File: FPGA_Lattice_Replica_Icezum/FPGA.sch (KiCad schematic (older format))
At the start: 33 parts, among them U1 iCE40HX1K-TQ144, U2 N25Q032A

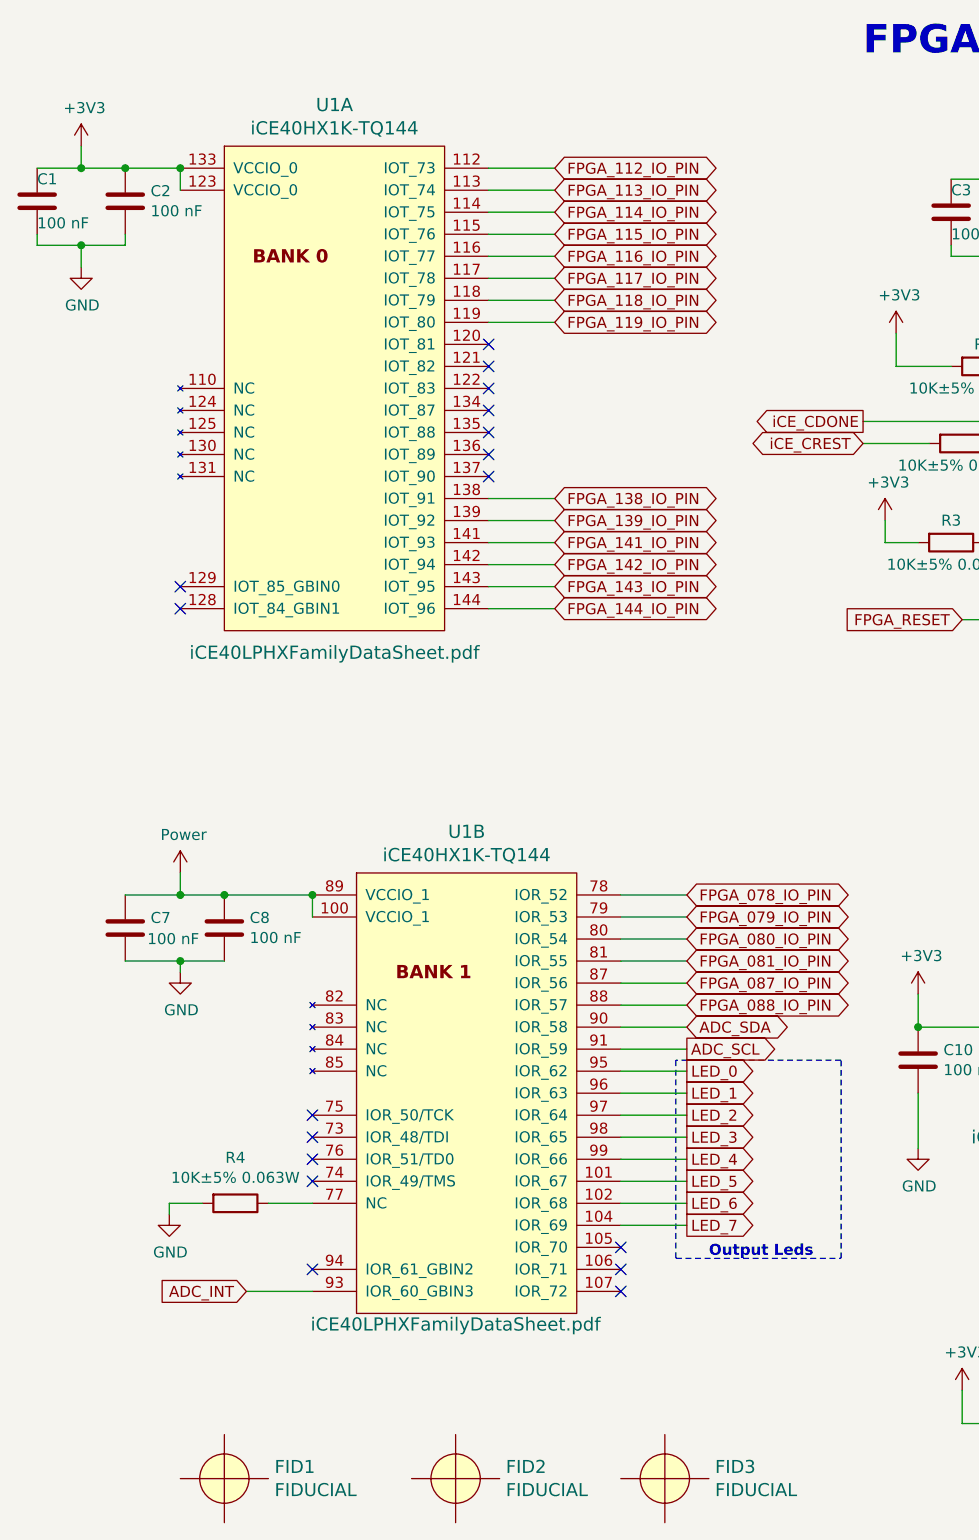
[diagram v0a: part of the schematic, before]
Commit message: se mejoro esquematico de acuerdo a la revisión del docente. Se mejoro rotulo (se coloco link del repo, autor y autor de la versión original y la licencia) se mejoro el flujo izquiera derecha de los botones, se desplazo fiduciales a la página principal, se achico el esquematico en la parte de headers
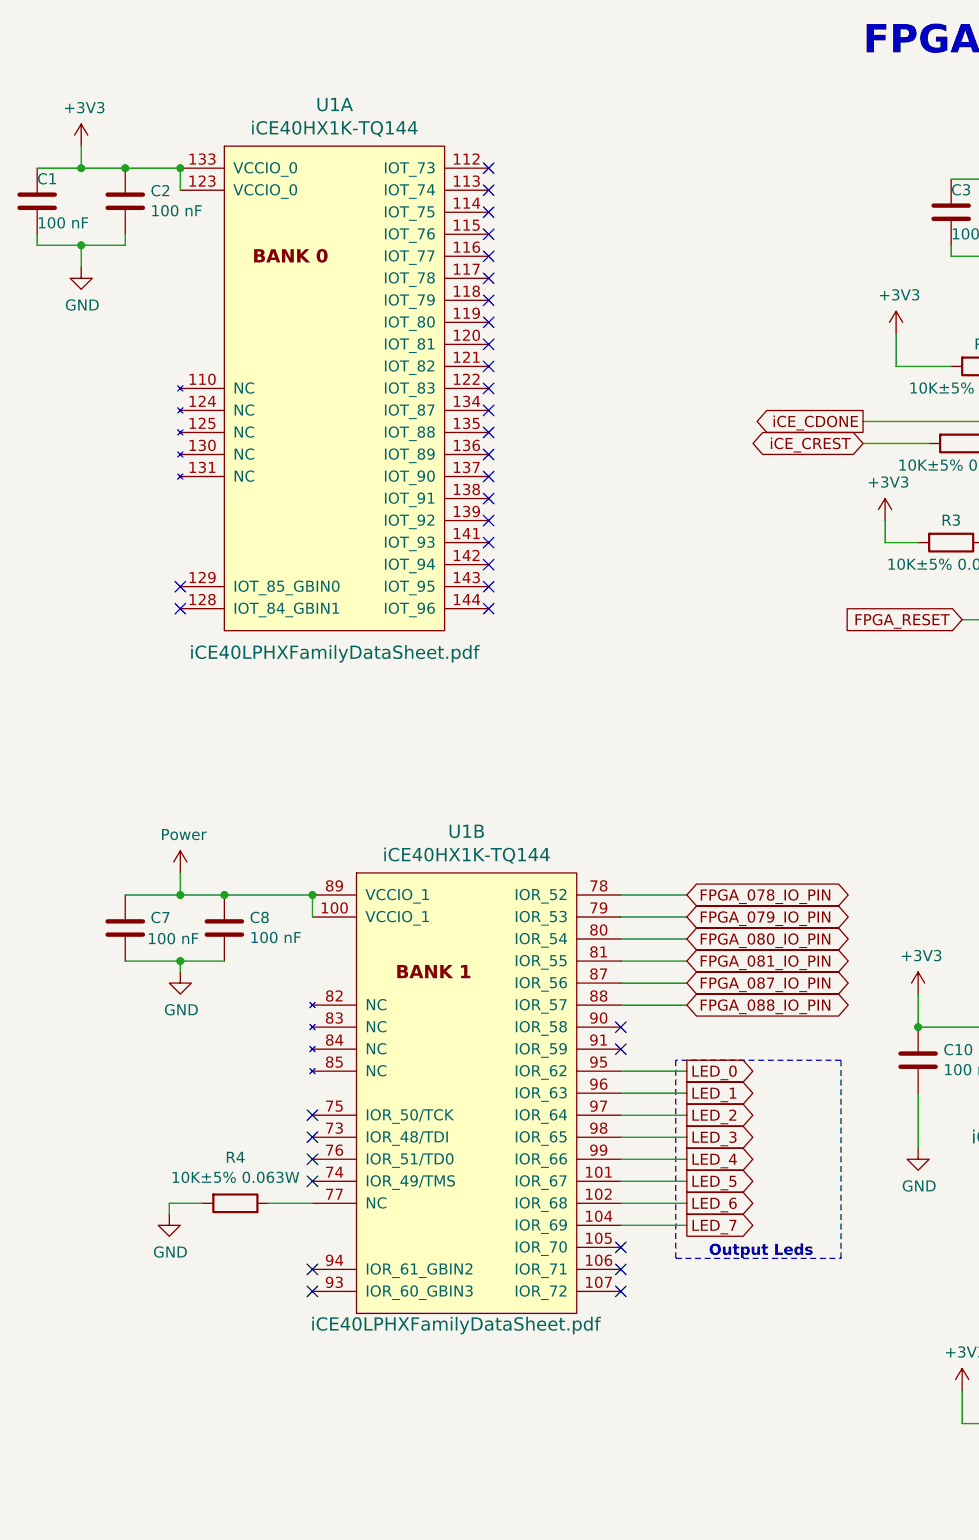
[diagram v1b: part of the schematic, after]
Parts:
- removed FID1, FID2, FID3: FIDUCIAL, footprints:Fiducial, symbol icezum:FIDUCIAL
- C1, C10, C2, C3, C4, C5, C6, C7, C8, C9: footprint footprints:C_0402 -> footprints:F_0805
- C11: footprint footprints:C_0603 -> footprints:L_0805
- C12, C13, C14, C15, C16: footprint footprints:C_0402 -> footprints:L_0805
- R1, R2, R3, R4, R46, R5, R6, R7, R8, R9: footprint footprints:R_0402 -> footprints:F_0805
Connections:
- net ADC_INT: no longer names the net of U1.93 (IOR_60_GBIN3)
- net ADC_SCL: no longer names the net of U1.91 (IOR_59)
- net ADC_SDA: no longer names the net of U1.90 (IOR_58)
- net FPGA_112_IO_PIN: no longer names the net of U1.112 (IOT_73)
- net FPGA_113_IO_PIN: no longer names the net of U1.113 (IOT_74)
- net FPGA_114_IO_PIN: no longer names the net of U1.114 (IOT_75)
- net FPGA_115_IO_PIN: no longer names the net of U1.115 (IOT_76)
- net FPGA_116_IO_PIN: no longer names the net of U1.116 (IOT_77)
- net FPGA_117_IO_PIN: no longer names the net of U1.117 (IOT_78)
- net FPGA_118_IO_PIN: no longer names the net of U1.118 (IOT_79)
- net FPGA_119_IO_PIN: no longer names the net of U1.119 (IOT_80)
- net FPGA_138_IO_PIN: no longer names the net of U1.138 (IOT_91)
- net FPGA_139_IO_PIN: no longer names the net of U1.139 (IOT_92)
- net FPGA_141_IO_PIN: no longer names the net of U1.141 (IOT_93)
- net FPGA_142_IO_PIN: no longer names the net of U1.142 (IOT_94)
- net FPGA_143_IO_PIN: no longer names the net of U1.143 (IOT_95)
- net FPGA_144_IO_PIN: no longer names the net of U1.144 (IOT_96)
- no-connect marks 44 -> 61
